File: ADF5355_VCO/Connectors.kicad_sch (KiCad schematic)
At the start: 3 parts, among them J1 Conn_01x02, J2 USB_B_Micro, SW1 SW_SPST

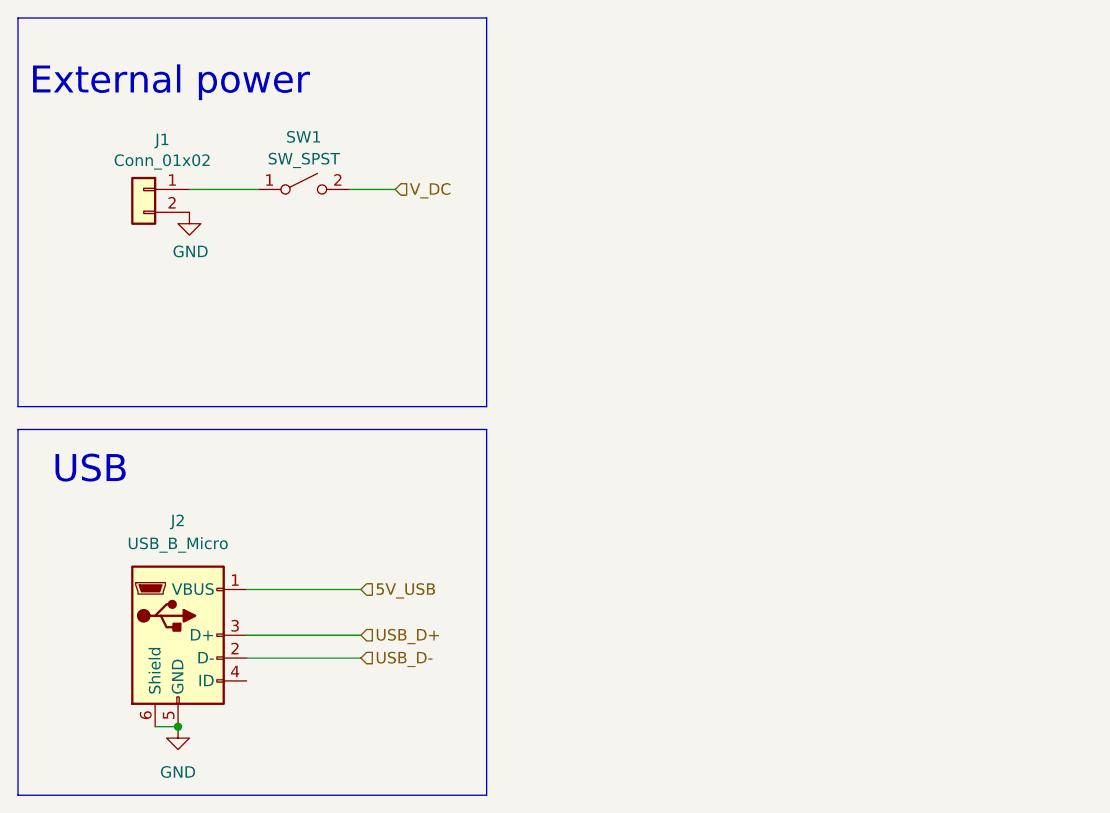
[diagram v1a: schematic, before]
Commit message: Added RF connectors
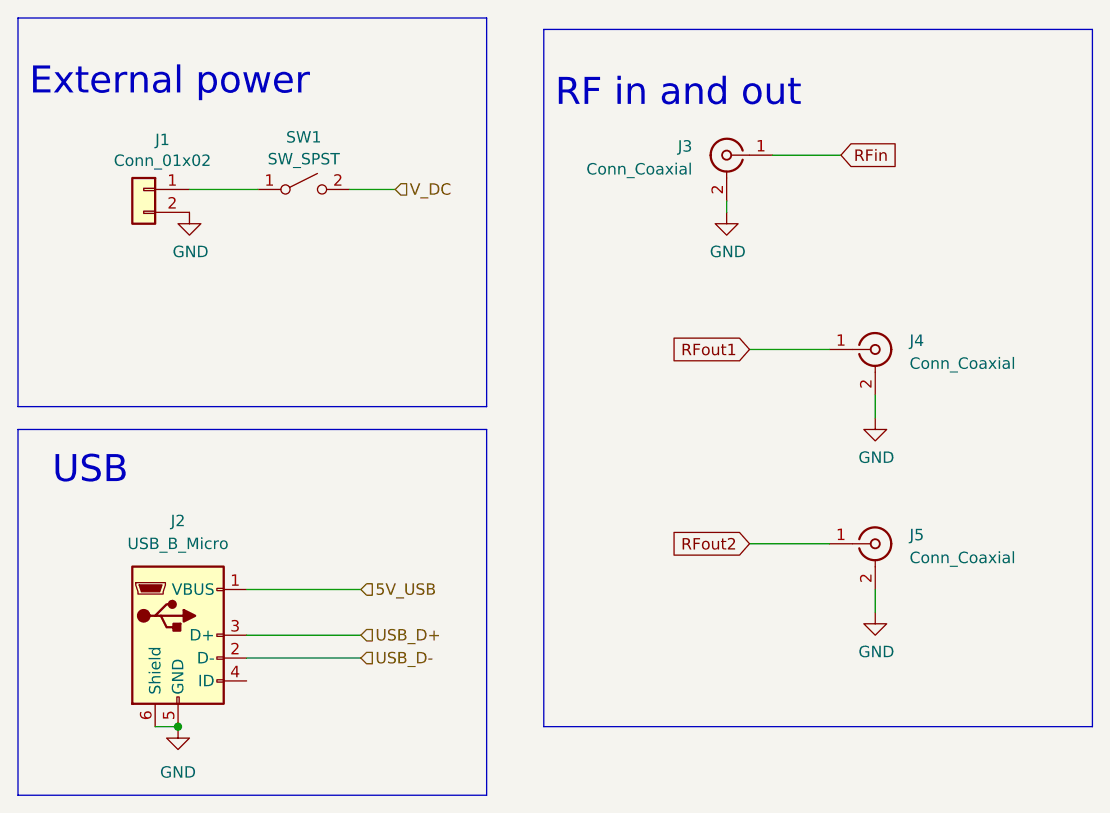
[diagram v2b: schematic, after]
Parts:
- added J3, J4, J5: Conn_Coaxial, symbol Connector:Conn_Coaxial
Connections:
- net GND: now also J3.2 (Ext), J4.2 (Ext), J5.2 (Ext)
- new net RFin: J3.1 (In)
- new net RFout1: J4.1 (In)
- new net RFout2: J5.1 (In)
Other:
- note added: "RF in and out"
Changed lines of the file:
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@@
+    (stroke (width 0) (type default))
+  )
+  (wire (pts (xy 115.57 60.96) (xy 115.57 59.69))
+    (stroke (width 0) (type default))
+  )
+  (wire (pts (xy 118.11 97.79) (xy 127 97.79))
     (stroke (width 0) (type default))
   )
@@
     (stroke (width 0) (type default))
   )
+  (wire (pts (xy 118.11 76.2) (xy 127 76.2))
+    (stroke (width 0) (type default))
+  )
   (wire (pts (xy 74.93 102.87) (xy 62.23 102.87))
     (stroke (width 0) (type default))
@@
     (stroke (width 0) (type default))
   )
+  (wire (pts (xy 120.65 54.61) (xy 128.27 54.61))
+    (stroke (width 0) (type default))
+  )
   (wire (pts (xy 55.88 58.42) (xy 63.5 58.42))
     (stroke (width 0) (type default))
   )
+  (wire (pts (xy 132.08 83.82) (xy 132.08 81.28))
+    (stroke (width 0) (type default))
+  )
   (wire (pts (xy 52.07 118.11) (xy 54.61 118.11))
     (stroke (width 0) (type default))
   )
+  (wire (pts (xy 132.08 105.41) (xy 132.08 102.87))
+    (stroke (width 0) (type default))
+  )
   (rectangle (start 36.83 39.37) (end 88.9 82.55)
     (stroke (width 0) (type default))
@@
     (stroke (width 0) (type default))
     (fill (type none))
+  )
+  (rectangle (start 95.25 40.64) (end 156.21 118.11)
+    (stroke (width 0) (type default))
+    (fill (type none))
+  )
+  (text "RF in and out\n" (at 96.52 49.53 0)
+    (effects (font (size 3 3)) (justify left bottom))
   )
   (text "External power" (at 38.1 48.26 0)
@@
   (text "USB" (at 40.64 91.44 0)
     (effects (font (size 3 3)) (justify left bottom))
+  )
+  (global_label "RFin" (shape input) (at 128.27 54.61 0) (fields_autoplaced)
+    (effects (font (size 1.27 1.27)) (justify left))
+    (property "Intersheetrefs" "${INTERSHEET_REFS}" (at 134.634 54.61 0)
+      (effects (font (size 1.27 1.27)) (justify left) hide)
+    )
+  )
+  (global_label "RFout2" (shape input) (at 118.11 97.79 180) (fields_autoplaced)
+    (effects (font (size 1.27 1.27)) (justify right))
+    (property "Intersheetrefs" "${INTERSHEET_REFS}" (at 109.2666 97.79 0)
+      (effects (font (size 1.27 1.27)) (justify right) hide)
+    )
+  )
+  (global_label "RFout1" (shape input) (at 118.11 76.2 180) (fields_autoplaced)
+    (effects (font (size 1.27 1.27)) (justify right))
+    (property "Intersheetrefs" "${INTERSHEET_REFS}" (at 109.2666 76.2 0)
+      (effects (font (size 1.27 1.27)) (justify right) hide)
+    )
   )
   (hierarchical_label "USB_D-" (shape input) (at 74.93 110.49 0) (fields_autoplaced)
@@
         (path "/29349b68-071c-451b-9b1e-10b5ef7e12a6/e8aaa04a-3e0b-4fcc-9719-a58df410b7e1"
           (reference "#PWR015") (unit 1)
+        )
+      )
+    )
+  )
+  (symbol (lib_id "power:GND") (at 115.57 60.96 0) (unit 1)
+    (in_bom yes) (on_board yes) (dnp no)
+    (property "Reference" "#PWR?" (at 115.57 67.31 0)
+      (effects (font (size 1.27 1.27)) hide)
+    )
+    (property "Value" "GND" (at 115.697 65.3542 0)
+      (effects (font (size 1.27 1.27)))
+    )
+    (property "Footprint" "" (at 115.57 60.96 0)
+      (effects (font (size 1.27 1.27)) hide)
+    )
+    (property "Datasheet" "" (at 115.57 60.96 0)
+      (effects (font (size 1.27 1.27)) hide)
+    )
+    (pin "1")
+    (instances
+      (project "ADF5355_VCO"
+        (path "/29349b68-071c-451b-9b1e-10b5ef7e12a6/00000000-0000-0000-0000-000064ac72b7"
+          (reference "#PWR?") (unit 1)
+        )
+        (path "/29349b68-071c-451b-9b1e-10b5ef7e12a6/e8aaa04a-3e0b-4fcc-9719-a58df410b7e1"
+          (reference "#PWR044") (unit 1)
         )
       )
@@
     )
   )
+  (symbol (lib_id "Connector:Conn_Coaxial") (at 132.08 97.79 0) (unit 1)
+    (in_bom yes) (on_board yes) (dnp no)
+    (property "Reference" "J5" (at 135.89 96.8132 0)
+      (effects (font (size 1.27 1.27)) (justify left))
+    )
+    (property "Value" "Conn_Coaxial" (at 135.89 99.3532 0)
+      (effects (font (size 1.27 1.27)) (justify left))
+    )
+    (property "Footprint" "" (at 132.08 97.79 0)
+      (effects (font (size 1.27 1.27)) hide)
+    )
+    (property "Datasheet" " ~" (at 132.08 97.79 0)
+      (effects (font (size 1.27 1.27)) hide)
+    )
+    (pin "1")
+    (pin "2")
+    (instances
+      (project "ADF5355_VCO"
+        (path "/29349b68-071c-451b-9b1e-10b5ef7e12a6/e8aaa04a-3e0b-4fcc-9719-a58df410b7e1"
+          (reference "J5") (unit 1)
+        )
+      )
+    )
+  )
   (symbol (lib_id "Switch:SW_SPST") (at 68.58 58.42 0) (unit 1)
     (in_bom yes) (on_board yes) (dnp no) (fields_autoplaced)
@@
     )
   )
+  (symbol (lib_id "power:GND") (at 132.08 105.41 0) (unit 1)
+    (in_bom yes) (on_board yes) (dnp no)
+    (property "Reference" "#PWR?" (at 132.08 111.76 0)
+      (effects (font (size 1.27 1.27)) hide)
+    )
+    (property "Value" "GND" (at 132.207 109.8042 0)
+      (effects (font (size 1.27 1.27)))
+    )
+    (property "Footprint" "" (at 132.08 105.41 0)
+      (effects (font (size 1.27 1.27)) hide)
+    )
+    (property "Datasheet" "" (at 132.08 105.41 0)
+      (effects (font (size 1.27 1.27)) hide)
+    )
+    (pin "1")
+    (instances
+      (project "ADF5355_VCO"
+        (path "/29349b68-071c-451b-9b1e-10b5ef7e12a6/00000000-0000-0000-0000-000064ac72b7"
+          (reference "#PWR?") (unit 1)
+        )
+        (path "/29349b68-071c-451b-9b1e-10b5ef7e12a6/e8aaa04a-3e0b-4fcc-9719-a58df410b7e1"
+          (reference "#PWR046") (unit 1)
+        )
+      )
+    )
+  )
+  (symbol (lib_id "Connector:Conn_Coaxial") (at 132.08 76.2 0) (unit 1)
+    (in_bom yes) (on_board yes) (dnp no)
+    (property "Reference" "J4" (at 135.89 75.2232 0)
+      (effects (font (size 1.27 1.27)) (justify left))
+    )
+    (property "Value" "Conn_Coaxial" (at 135.89 77.7632 0)
+      (effects (font (size 1.27 1.27)) (justify left))
+    )
+    (property "Footprint" "" (at 132.08 76.2 0)
+      (effects (font (size 1.27 1.27)) hide)
+    )
+    (property "Datasheet" " ~" (at 132.08 76.2 0)
+      (effects (font (size 1.27 1.27)) hide)
+    )
+    (pin "1")
+    (pin "2")
+    (instances
+      (project "ADF5355_VCO"
+        (path "/29349b68-071c-451b-9b1e-10b5ef7e12a6/e8aaa04a-3e0b-4fcc-9719-a58df410b7e1"
+          (reference "J4") (unit 1)
+        )
+      )
+    )
+  )
   (symbol (lib_id "power:GND") (at 55.88 60.96 0) (unit 1)
     (in_bom yes) (on_board yes) (dnp no)
@@
         )
       )
+    )
+  )
+  (symbol (lib_id "Connector:Conn_Coaxial") (at 115.57 54.61 0) (mirror y) (unit 1)
+    (in_bom yes) (on_board yes) (dnp no)
+    (property "Reference" "J3" (at 111.76 53.6332 0)
+      (effects (font (size 1.27 1.27)) (justify left))
+    )
+    (property "Value" "Conn_Coaxial" (at 111.76 56.1732 0)
+      (effects (font (size 1.27 1.27)) (justify left))
+    )
+    (property "Footprint" "" (at 115.57 54.61 0)
+      (effects (font (size 1.27 1.27)) hide)
+    )
+    (property "Datasheet" " ~" (at 115.57 54.61 0)
+      (effects (font (size 1.27 1.27)) hide)
+    )
+    (pin "1")
+    (pin "2")
+    (instances
+      (project "ADF5355_VCO"
+        (path "/29349b68-071c-451b-9b1e-10b5ef7e12a6/e8aaa04a-3e0b-4fcc-9719-a58df410b7e1"
+          (reference "J3") (unit 1)
+        )
+      )
+    )
+  )
+  (symbol (lib_id "power:GND") (at 132.08 83.82 0) (unit 1)
+    (in_bom yes) (on_board yes) (dnp no)
+    (property "Reference" "#PWR?" (at 132.08 90.17 0)
+      (effects (font (size 1.27 1.27)) hide)
+    )
+    (property "Value" "GND" (at 132.207 88.2142 0)
+      (effects (font (size 1.27 1.27)))
+    )
+    (property "Footprint" "" (at 132.08 83.82 0)
+      (effects (font (size 1.27 1.27)) hide)
+    )
+    (property "Datasheet" "" (at 132.08 83.82 0)
+      (effects (font (size 1.27 1.27)) hide)
+    )
+    (pin "1")
+    (instances
+      (project "ADF5355_VCO"
+        (path "/29349b68-071c-451b-9b1e-10b5ef7e12a6/00000000-0000-0000-0000-000064ac72b7"
+          (reference "#PWR?") (unit 1)
+        )
+        (path "/29349b68-071c-451b-9b1e-10b5ef7e12a6/e8aaa04a-3e0b-4fcc-9719-a58df410b7e1"
+          (reference "#PWR045") (unit 1)
+        )
+      )

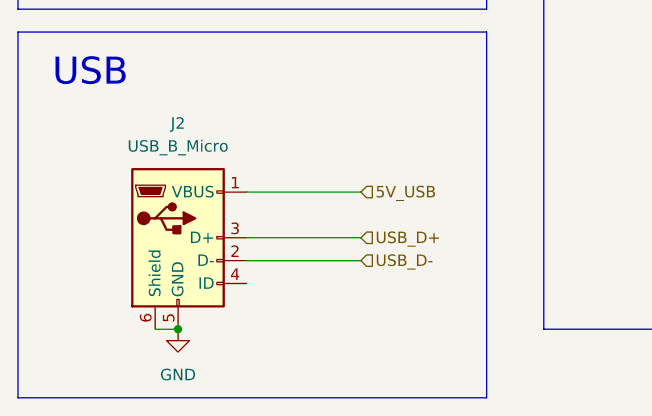
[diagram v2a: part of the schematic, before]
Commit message: Added footprints to some components
Footprints added for:
SMA connectors
DC banana connector
USB connector
LCD screen
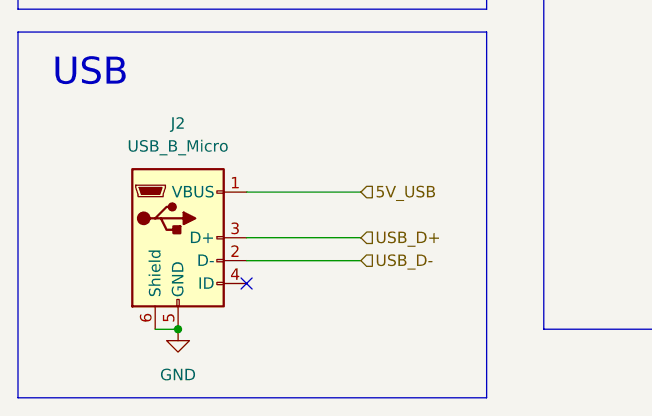
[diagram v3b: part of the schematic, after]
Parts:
- J1: footprint (none) -> Connector:Banana_Cliff_FCR7350x_S16N-PC_Horizontal
- J2: footprint (none) -> Connector_USB:USB_Micro-B_Molex-105133-0001
- J3, J4, J5: footprint (none) -> Connector_Coaxial:SMA_Molex_73251-1153_EdgeMount_Horizontal
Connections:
- no-connect marks 0 -> 1
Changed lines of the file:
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@@
   (junction (at 54.61 118.11) (diameter 0) (color 0 0 0 0)
   )
+  (no_connect (at 62.23 113.03))
   (wire (pts (xy 74.93 110.49) (xy 62.23 110.49))
     (stroke (width 0) (type default))
@@
       (effects (font (size 1.27 1.27)))
     )
-    (property "Footprint" "" (at 58.42 109.22 0)
+    (property "Footprint" "Connector_USB:USB_Micro-B_Molex-105133-0001" (at 58.42 109.22 0)
       (effects (font (size 1.27 1.27)) hide)
     )
@@
       (effects (font (size 1.27 1.27)) (justify left))
     )
-    (property "Footprint" "" (at 132.08 97.79 0)
-      (effects (font (size 1.27 1.27)) hide)
-    )
-    (property "Datasheet" " ~" (at 132.08 97.79 0)
+    (property "Footprint" "Connector_Coaxial:SMA_Molex_73251-1153_EdgeMount_Horizontal" (at 132.08 97.79 0)
+      (effects (font (size 1.27 1.27)) hide)
+    )
+    (property "Datasheet" "https://www.molex.com/content/dam/molex/molex-dot-com/products/automated/en-us/salesdrawingpdf/732/73251/732511153_sd.pdf" (at 132.08 97.79 0)
       (effects (font (size 1.27 1.27)) hide)
     )
@@
       (effects (font (size 1.27 1.27)))
     )
-    (property "Footprint" "" (at 50.8 58.42 0)
+    (property "Footprint" "Connector:Banana_Cliff_FCR7350x_S16N-PC_Horizontal" (at 50.8 58.42 0)
       (effects (font (size 1.27 1.27)) hide)
     )
@@
       (effects (font (size 1.27 1.27)) (justify left))
     )
-    (property "Footprint" "" (at 132.08 76.2 0)
-      (effects (font (size 1.27 1.27)) hide)
-    )
-    (property "Datasheet" " ~" (at 132.08 76.2 0)
+    (property "Footprint" "Connector_Coaxial:SMA_Molex_73251-1153_EdgeMount_Horizontal" (at 132.08 76.2 0)
+      (effects (font (size 1.27 1.27)) hide)
+    )
+    (property "Datasheet" "https://www.molex.com/content/dam/molex/molex-dot-com/products/automated/en-us/salesdrawingpdf/732/73251/732511153_sd.pdf" (at 132.08 76.2 0)
       (effects (font (size 1.27 1.27)) hide)
     )
@@
       (effects (font (size 1.27 1.27)) (justify left))
     )
-    (property "Footprint" "" (at 115.57 54.61 0)
-      (effects (font (size 1.27 1.27)) hide)
-    )
-    (property "Datasheet" " ~" (at 115.57 54.61 0)
-      (effects (font (size 1.27 1.27)) hide)
-    )
+    (property "Footprint" "Connector_Coaxial:SMA_Molex_73251-1153_EdgeMount_Horizontal" (at 115.57 54.61 0)
+      (effects (font (size 1.27 1.27)) hide)
+    )
+    (property "Datasheet" "https://www.molex.com/content/dam/molex/molex-dot-com/products/automated/en-us/salesdrawingpdf/732/73251/732511153_sd.pdf" (at 115.57 54.61 0)
+      (effects (font (size 1.27 1.27)) hide)
+    )

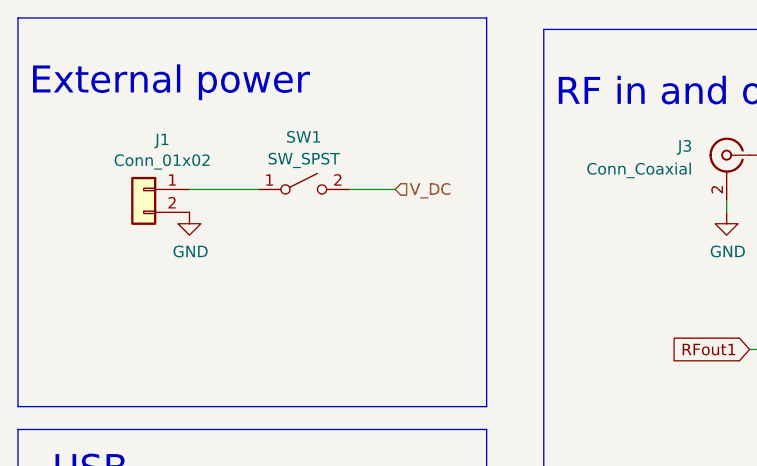
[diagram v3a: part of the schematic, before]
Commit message: Added additional footprints and BOM
Added a bill of materials with most of the components.
Added footprints for more components
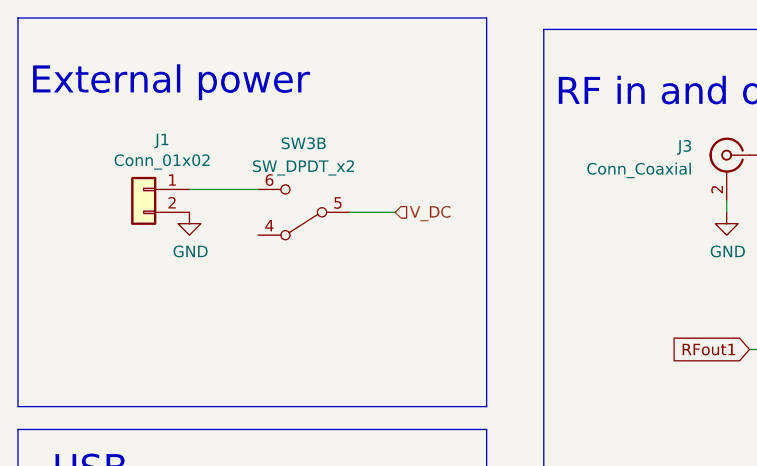
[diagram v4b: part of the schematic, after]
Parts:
- removed SW1: SW_SPST, symbol Switch:SW_SPST
- added SW3: SW_DPDT_x2, symbol Switch:SW_DPDT_x2
- J2: footprint Connector_USB:USB_Micro-B_Molex-105133-0001 -> Connector_USB:USB_Micro-B_Amphenol_10118194_Horizontal
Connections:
- net V_DC: now also SW3.5 (B)
- net at J1.1 (Pin_1): now also SW3.6 (C)
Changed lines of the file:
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@@
+    (stroke (width 0) (type default))
+  )
+  (wire (pts (xy 73.66 60.96) (xy 78.74 60.96))
     (stroke (width 0) (type default))
   )
@@
   )
   (wire (pts (xy 74.93 102.87) (xy 62.23 102.87))
-    (stroke (width 0) (type default))
-  )
-  (wire (pts (xy 73.66 58.42) (xy 78.74 58.42))
     (stroke (width 0) (type default))
   )
@@
     (effects (font (size 1.27 1.27)) (justify left))
   )
-  (hierarchical_label "V_DC" (shape input) (at 78.74 58.42 0) (fields_autoplaced)
+  (hierarchical_label "V_DC" (shape input) (at 78.74 60.96 0) (fields_autoplaced)
     (effects (font (size 1.27 1.27)) (justify left))
   )
@@
       (effects (font (size 1.27 1.27)))
     )
-    (property "Footprint" "Connector_USB:USB_Micro-B_Molex-105133-0001" (at 58.42 109.22 0)
+    (property "Footprint" "Connector_USB:USB_Micro-B_Amphenol_10118194_Horizontal" (at 58.42 109.22 0)
       (effects (font (size 1.27 1.27)) hide)
     )
@@
     )
   )
-  (symbol (lib_id "Switch:SW_SPST") (at 68.58 58.42 0) (unit 1)
+  (symbol (lib_id "Switch:SW_DPDT_x2") (at 68.58 60.96 180) (unit 2)
     (in_bom yes) (on_board yes) (dnp no) (fields_autoplaced)
-    (property "Reference" "SW1" (at 68.58 52.6247 0)
-      (effects (font (size 1.27 1.27)))
-    )
-    (property "Value" "SW_SPST" (at 68.58 55.0489 0)
-      (effects (font (size 1.27 1.27)))
-    )
-    (property "Footprint" "" (at 68.58 58.42 0)
-      (effects (font (size 1.27 1.27)) hide)
-    )
-    (property "Datasheet" "~" (at 68.58 58.42 0)
+    (property "Reference" "SW3" (at 68.58 53.34 0)
+      (effects (font (size 1.27 1.27)))
+    )
+    (property "Value" "SW_DPDT_x2" (at 68.58 55.88 0)
+      (effects (font (size 1.27 1.27)))
+    )
+    (property "Footprint" "" (at 68.58 60.96 0)
+      (effects (font (size 1.27 1.27)) hide)
+    )
+    (property "Datasheet" "~" (at 68.58 60.96 0)
       (effects (font (size 1.27 1.27)) hide)
     )
     (pin "1")
     (pin "2")
-    (instances
-      (project "ADF5355_VCO"
-        (path "/29349b68-071c-451b-9b1e-10b5ef7e12a6/00000000-0000-0000-0000-000064ac72b7"
-          (reference "SW1") (unit 1)
-        )
-        (path "/29349b68-071c-451b-9b1e-10b5ef7e12a6/e8aaa04a-3e0b-4fcc-9719-a58df410b7e1"
-          (reference "SW1") (unit 1)
-        )
-      )
+    (pin "3")
+    (pin "4")
+    (pin "5")
+    (pin "6")
+    (instances
+      (project "ADF5355_VCO"
+        (path "/29349b68-071c-451b-9b1e-10b5ef7e12a6/8e6d62a1-615e-4e74-ad33-9284c4715f87"
+          (reference "SW3") (unit 2)
+        )
+        (path "/29349b68-071c-451b-9b1e-10b5ef7e12a6/e8aaa04a-3e0b-4fcc-9719-a58df410b7e1"
+          (reference "SW1") (unit 2)
+        )
+      )
